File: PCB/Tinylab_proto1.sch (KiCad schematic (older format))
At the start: 73 parts, among them IC1 ATXMEGA16A4U-A, P1 SCOPE_OUT, P10 EXPANSION, P11 SWITCH, P2 USB_OTG, P3 DIG_OUT, P4 PDI/3V3, P5 SCOPE_OUT, P6 DAC_OUT, P7 PSU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

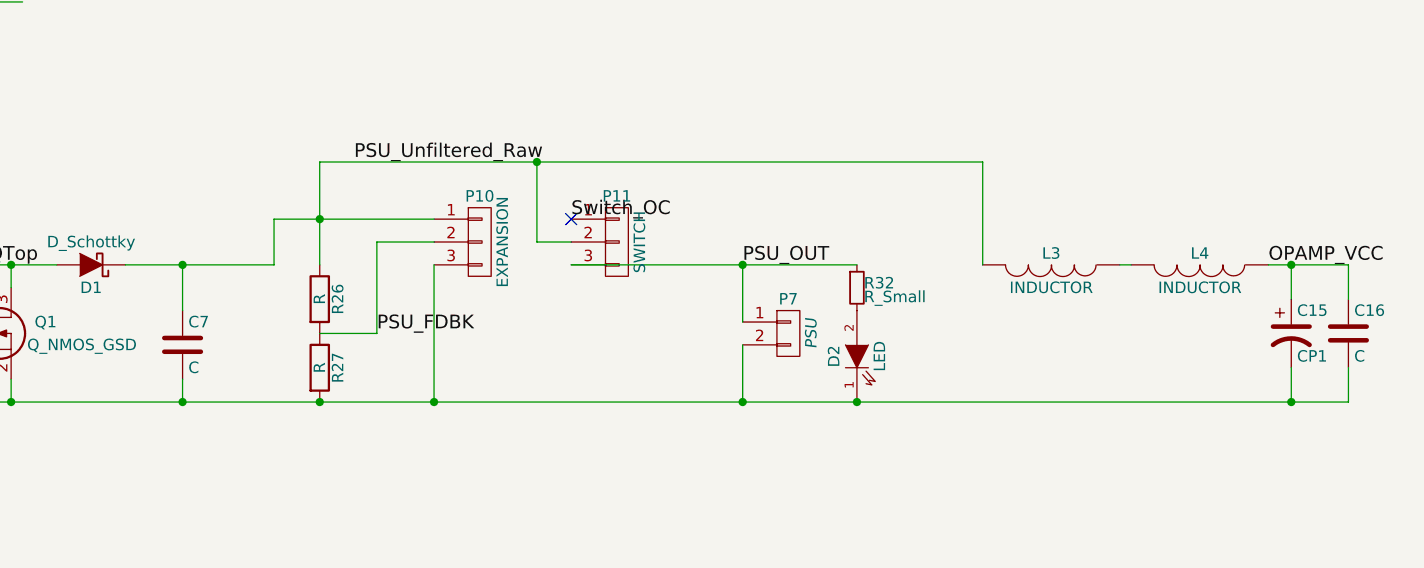
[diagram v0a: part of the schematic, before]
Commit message: Redoing the board
Signal gen and PSU wired in.  Very happy!
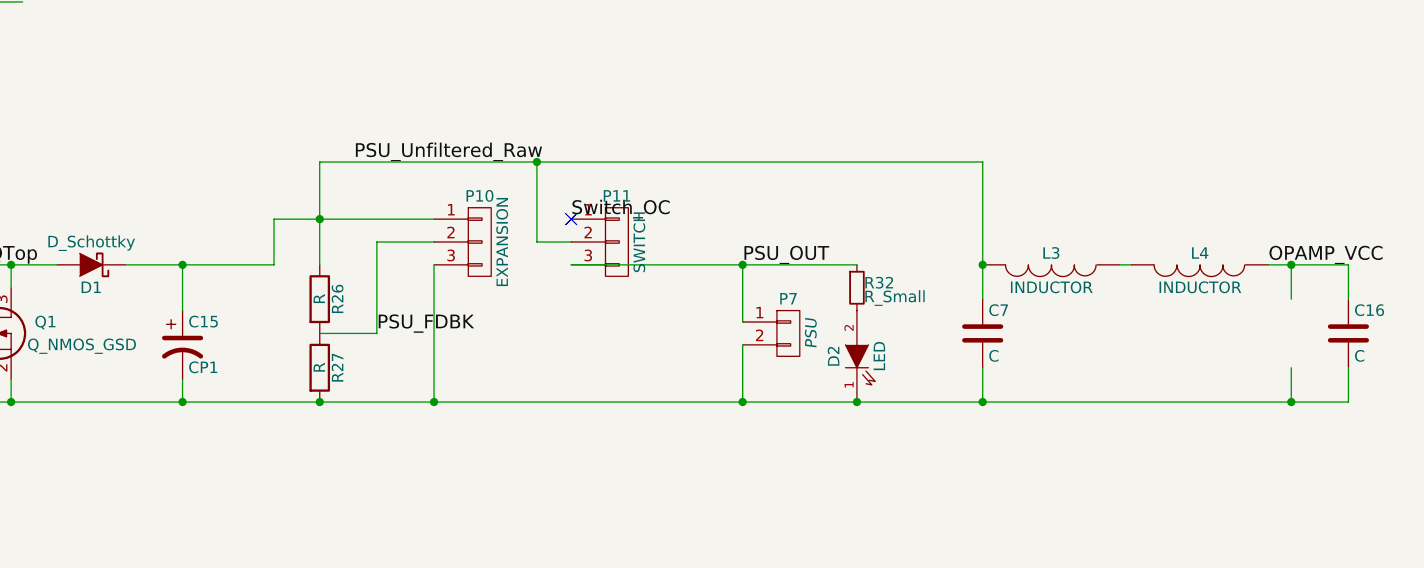
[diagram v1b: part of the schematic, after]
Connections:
- net OPAMP_VCC: no longer C15.1
- net PSU_Unfiltered_Raw: now also C15.1
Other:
- moved on the sheet: C15, C7
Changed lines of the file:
@@
 L CP1 C15
 U 1 1 560735FE
-P 16350 5350
-F 0 "C15" H 16375 5450 50  0000 L CNN
-F 1 "CP1" H 16375 5250 50  0000 L CNN
-F 2 "Capacitors_SMD:c_elec_4x5.3" H 16350 5350 60  0001 C CNN
-F 3 "" H 16350 5350 60  0000 C CNN
-	1    16350 5350
+P 11500 5400
+F 0 "C15" H 11525 5500 50  0000 L CNN
+F 1 "CP1" H 11525 5300 50  0000 L CNN
+F 2 "Capacitors_SMD:c_elec_4x5.3" H 11500 5400 60  0001 C CNN
+F 3 "" H 11500 5400 60  0000 C CNN
+	1    11500 5400
 	1    0    0    -1
 $EndComp
@@
 L C C7
 U 1 1 56E8E263
-P 11500 5400
-F 0 "C7" H 11525 5500 50  0000 L CNN
-F 1 "C" H 11525 5300 50  0000 L CNN
-F 2 "Capacitors_SMD:C_0603" H 11538 5250 30  0001 C CNN
-F 3 "" H 11500 5400 60  0000 C CNN
-	1    11500 5400
+P 15000 5350
+F 0 "C7" H 15025 5450 50  0000 L CNN
+F 1 "C" H 15025 5250 50  0000 L CNN
+F 2 "Capacitors_SMD:C_0603" H 15038 5200 30  0001 C CNN
+F 3 "" H 15000 5350 60  0000 C CNN
+	1    15000 5350
 	1    0    0    -1
 $EndComp
@@
 	16600 5050 16600 5200
 Wire Wire Line
-	16350 5200 16350 5050
-Wire Wire Line
-	16350 5650 16350 5500
-Wire Wire Line
 	12100 5350 12350 5350
 Connection ~ 10300 5350
@@
 	12100 4600 15000 4600
 Wire Wire Line
-	15000 4600 15000 5050
+	15000 4600 15000 5200
 Wire Wire Line
 	12100 4600 12100 5050
@@
 Text Label 11000 11550 0    60   ~ 0
 R23-R25
+Connection ~ 15000 5050
+Wire Wire Line
+	15000 5500 15000 5650
+Connection ~ 15000 5650
+Wire Wire Line
+	16350 5200 16350 5050
+Wire Wire Line
+	16350 5500 16350 5650
 $EndSCHEMATC

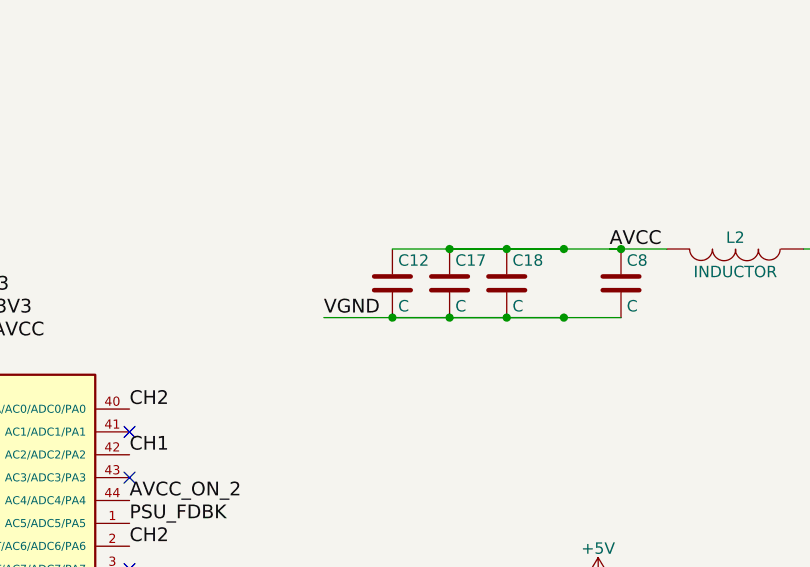
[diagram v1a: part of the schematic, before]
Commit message: FInished the board.
Just need to position balange pins.  Design seems tight, with really low
power supply distances.
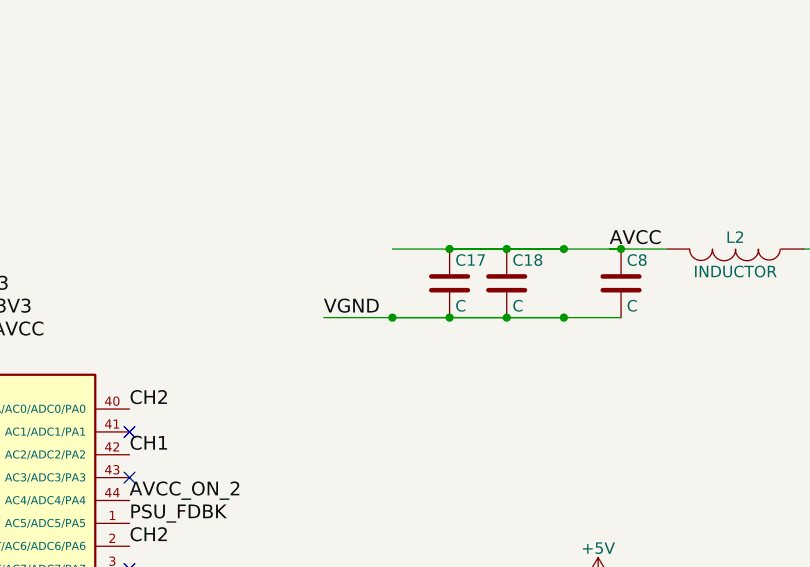
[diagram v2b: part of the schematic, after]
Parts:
- removed C12: C, Capacitors_SMD:C_0603, symbol C
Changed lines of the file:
@@
-$EndComp
-$Comp
-L C C12
-U 1 1 575646EC
-P 8200 3750
-F 0 "C12" H 8225 3850 50  0000 L CNN
-F 1 "C" H 8225 3650 50  0000 L CNN
-F 2 "Capacitors_SMD:C_0603" H 8238 3600 50  0001 C CNN
-F 3 "" H 8200 3750 50  0000 C CNN
-	1    8200 3750
-	1    0    0    -1
 $EndComp
 $Comp
@@
 Wire Wire Line
 	13950 5650 13950 5400
-Wire Wire Line
-	8200 3600 9200 3600
 Wire Wire Line
 	8450 3600 8950 3600
@@
 Wire Wire Line
 	16350 5500 16350 5650
+Wire Wire Line
+	8200 3600 9200 3600
 $EndSCHEMATC

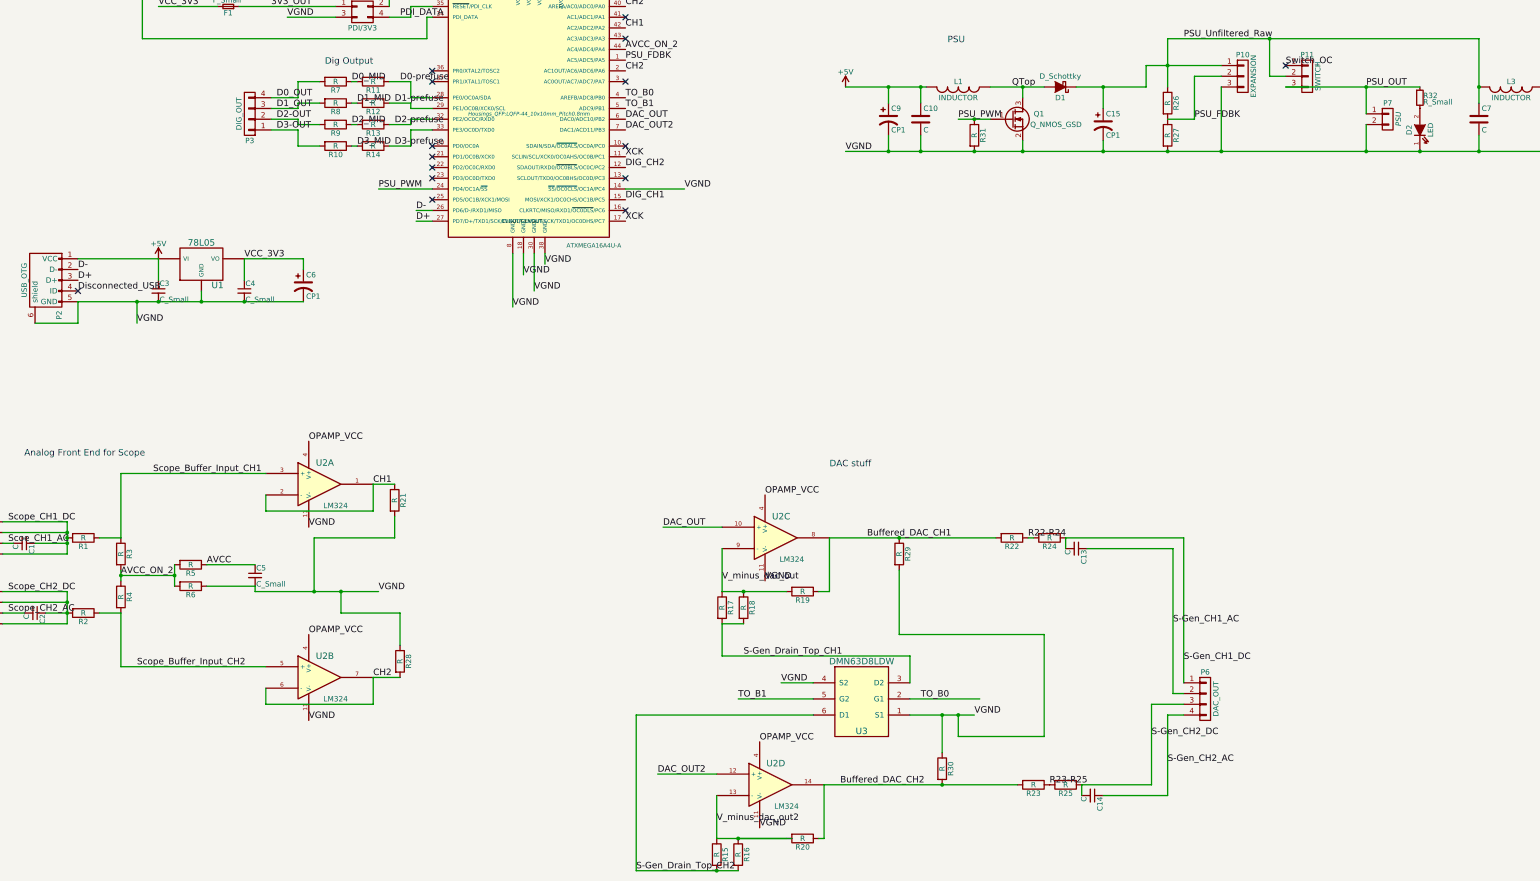
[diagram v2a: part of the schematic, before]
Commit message: Added more #defines to code
These #defines are located in desktop_settings.h and allow you to edit
how many samples are discarded per packet.  The idea was to use this to
test the MCU-side code and ensure that it doesn't corrupt a packet per
frame, but this seems to have magically disappeared (???).

I remember queueing USB transfers a long time ago, but can't remember
this having any success.  It's more likely to just be a random clock
skew issue that only appears on some boards - and it's only "fixed" on
the one particular test board I have in hand now.  I think.
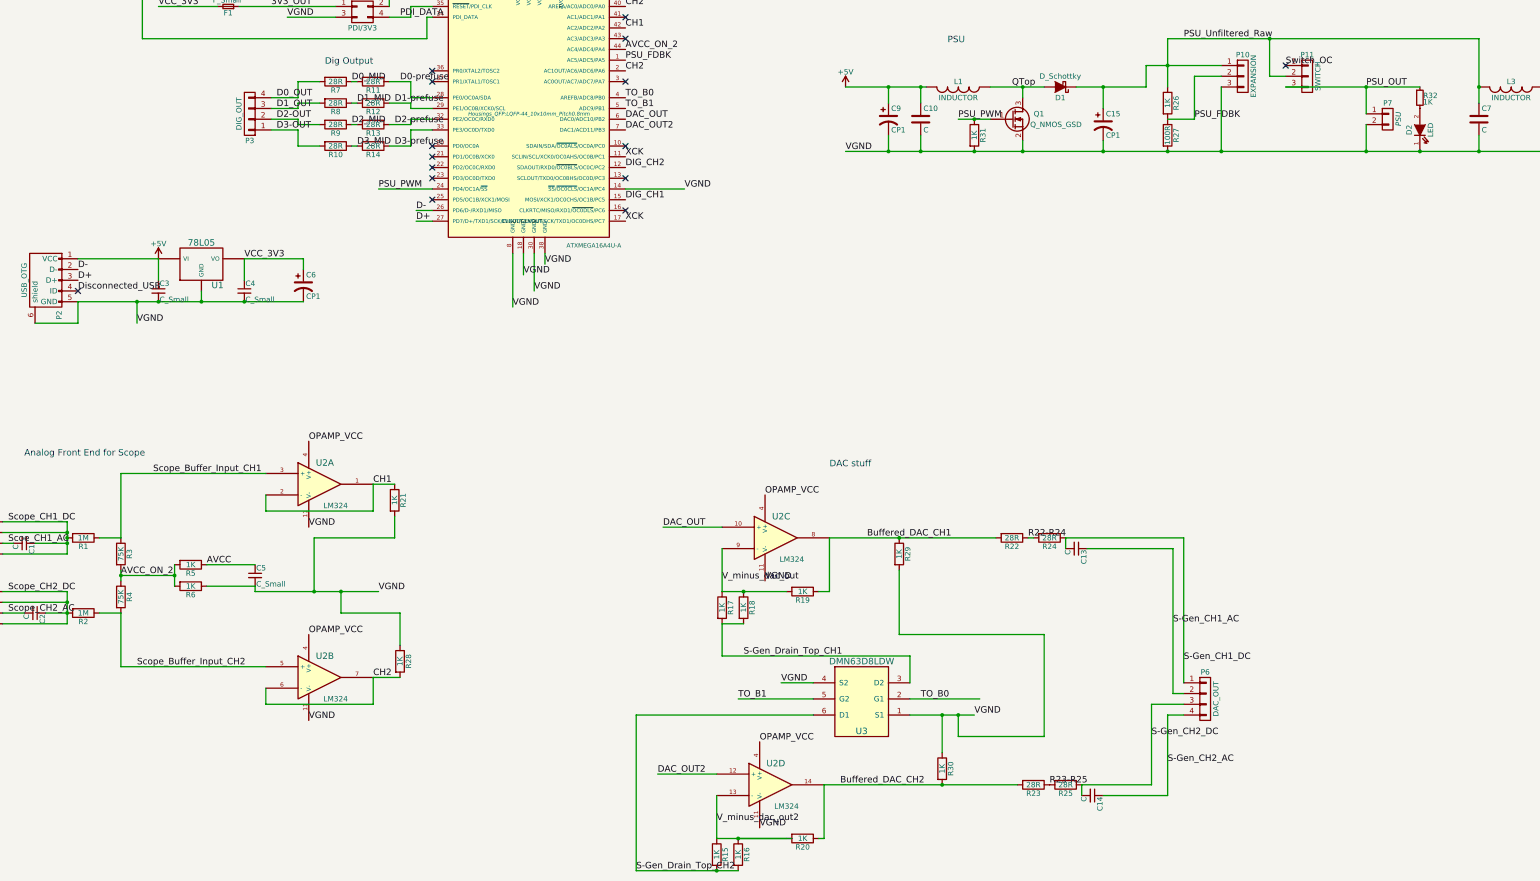
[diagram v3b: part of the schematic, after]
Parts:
- R1, R2: value R -> 1M
- R10, R11, R12, R13, R14, R22, R23, R24, R25, R7, R8, R9: value R -> 28R
- R15, R16, R17, R18, R19, R20, R21, R26, R28, R29, R30, R31, R5, R6: value R -> 1K
- R27: value R -> 100R
- R3, R4: value R -> 75K
- R32: value R_Small -> 1K
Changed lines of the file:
@@
 P 2000 9250
 F 0 "R1" V 2080 9250 50  0000 C CNN
-F 1 "R" V 2000 9250 50  0000 C CNN
+F 1 "1M" V 2000 9250 50  0000 C CNN
 F 2 "Resistors_SMD:R_0603" V 1930 9250 30  0001 C CNN
 F 3 "" H 2000 9250 30  0000 C CNN
@@
 P 2350 9400
 F 0 "R3" V 2430 9400 50  0000 C CNN
-F 1 "R" V 2350 9400 50  0000 C CNN
+F 1 "75K" V 2350 9400 50  0000 C CNN
 F 2 "Resistors_SMD:R_0603" V 2280 9400 30  0001 C CNN
 F 3 "" H 2350 9400 30  0000 C CNN
@@
 P 3000 9500
 F 0 "R5" V 3080 9500 50  0000 C CNN
-F 1 "R" V 3000 9500 50  0000 C CNN
+F 1 "1K" V 3000 9500 50  0000 C CNN
 F 2 "Resistors_SMD:R_0603" V 2930 9500 30  0001 C CNN
 F 3 "" H 3000 9500 30  0000 C CNN
@@
 P 3000 9700
 F 0 "R6" V 3080 9700 50  0000 C CNN
-F 1 "R" V 3000 9700 50  0000 C CNN
+F 1 "1K" V 3000 9700 50  0000 C CNN
 F 2 "Resistors_SMD:R_0603" V 2930 9700 30  0001 C CNN
 F 3 "" H 3000 9700 30  0000 C CNN
@@
 P 2350 9800
 F 0 "R4" V 2430 9800 50  0000 C CNN
-F 1 "R" V 2350 9800 50  0000 C CNN
+F 1 "75K" V 2350 9800 50  0000 C CNN
 F 2 "Resistors_SMD:R_0603" V 2280 9800 30  0001 C CNN
 F 3 "" H 2350 9800 30  0000 C CNN
@@
 P 2000 9950
 F 0 "R2" V 2080 9950 50  0000 C CNN
-F 1 "R" V 2000 9950 50  0000 C CNN
+F 1 "1M" V 2000 9950 50  0000 C CNN
 F 2 "Resistors_SMD:R_0603" V 1930 9950 30  0001 C CNN
 F 3 "" H 2000 9950 30  0000 C CNN
@@
 P 10650 9250
 F 0 "R22" V 10730 9250 50  0000 C CNN
-F 1 "R" V 10650 9250 50  0000 C CNN
+F 1 "28R" V 10650 9250 50  0000 C CNN
 F 2 "Resistors_SMD:R_0603" V 10580 9250 30  0001 C CNN
 F 3 "" H 10650 9250 30  0000 C CNN
@@
 P 11000 9250
 F 0 "R24" V 11080 9250 50  0000 C CNN
-F 1 "R" V 11000 9250 50  0000 C CNN
+F 1 "28R" V 11000 9250 50  0000 C CNN
 F 2 "Resistors_SMD:R_0603" V 10930 9250 30  0001 C CNN
 F 3 "" H 11000 9250 30  0000 C CNN
@@
 P 4700 5000
 F 0 "R11" V 4780 5000 50  0000 C CNN
-F 1 "R" V 4700 5000 50  0000 C CNN
+F 1 "28R" V 4700 5000 50  0000 C CNN
 F 2 "Resistors_SMD:R_0603" V 4630 5000 30  0001 C CNN
 F 3 "" H 4700 5000 30  0000 C CNN
@@
 P 4350 5000
 F 0 "R7" V 4430 5000 50  0000 C CNN
-F 1 "R" V 4350 5000 50  0000 C CNN
+F 1 "28R" V 4350 5000 50  0000 C CNN
 F 2 "Resistors_SMD:R_0603" V 4280 5000 30  0001 C CNN
 F 3 "" H 4350 5000 30  0000 C CNN
@@
 P 4700 5400
 F 0 "R13" V 4780 5400 50  0000 C CNN
-F 1 "R" V 4700 5400 50  0000 C CNN
+F 1 "28R" V 4700 5400 50  0000 C CNN
 F 2 "Resistors_SMD:R_0603" V 4630 5400 30  0001 C CNN
 F 3 "" H 4700 5400 30  0000 C CNN
@@
 P 4350 5400
 F 0 "R9" V 4430 5400 50  0000 C CNN
-F 1 "R" V 4350 5400 50  0000 C CNN
+F 1 "28R" V 4350 5400 50  0000 C CNN
 F 2 "Resistors_SMD:R_0603" V 4280 5400 30  0001 C CNN
 F 3 "" H 4350 5400 30  0000 C CNN
@@
 P 4700 5600
 F 0 "R14" V 4780 5600 50  0000 C CNN
-F 1 "R" V 4700 5600 50  0000 C CNN
+F 1 "28R" V 4700 5600 50  0000 C CNN
 F 2 "Resistors_SMD:R_0603" V 4630 5600 30  0001 C CNN
 F 3 "" H 4700 5600 30  0000 C CNN
@@
 P 4350 5600
 F 0 "R10" V 4430 5600 50  0000 C CNN
-F 1 "R" V 4350 5600 50  0000 C CNN
+F 1 "28R" V 4350 5600 50  0000 C CNN
 F 2 "Resistors_SMD:R_0603" V 4280 5600 30  0001 C CNN
 F 3 "" H 4350 5600 30  0000 C CNN
@@
 P 4700 5200
 F 0 "R12" V 4780 5200 50  0000 C CNN
-F 1 "R" V 4700 5200 50  0000 C CNN
+F 1 "28R" V 4700 5200 50  0000 C CNN
 F 2 "Resistors_SMD:R_0603" V 4630 5200 30  0001 C CNN
 F 3 "" H 4700 5200 30  0000 C CNN
@@
 P 4350 5200
 F 0 "R8" V 4430 5200 50  0000 C CNN
-F 1 "R" V 4350 5200 50  0000 C CNN
+F 1 "28R" V 4350 5200 50  0000 C CNN
 F 2 "Resistors_SMD:R_0603" V 4280 5200 30  0001 C CNN
 F 3 "" H 4350 5200 30  0000 C CNN
@@
 P 10850 11550
 F 0 "R23" V 10930 11550 50  0000 C CNN
-F 1 "R" V 10850 11550 50  0000 C CNN
+F 1 "28R" V 10850 11550 50  0000 C CNN
 F 2 "Resistors_SMD:R_0603" V 10780 11550 30  0001 C CNN
 F 3 "" H 10850 11550 30  0000 C CNN
@@
 P 11150 11550
 F 0 "R25" V 11230 11550 50  0000 C CNN
-F 1 "R" V 11150 11550 50  0000 C CNN
+F 1 "28R" V 11150 11550 50  0000 C CNN
 F 2 "Resistors_SMD:R_0603" V 11080 11550 30  0001 C CNN
 F 3 "" H 11150 11550 30  0000 C CNN
@@
 P 12100 5200
 F 0 "R26" V 12180 5200 50  0000 C CNN
-F 1 "R" V 12100 5200 50  0000 C CNN
+F 1 "1K" V 12100 5200 50  0000 C CNN
 F 2 "Resistors_SMD:R_0603" V 12030 5200 30  0001 C CNN
 F 3 "" H 12100 5200 30  0000 C CNN
@@
 P 12100 5500
 F 0 "R27" V 12180 5500 50  0000 C CNN
-F 1 "R" V 12100 5500 50  0000 C CNN
+F 1 "100R" V 12100 5500 50  0000 C CNN
 F 2 "Resistors_SMD:R_0603" V 12030 5500 30  0001 C CNN
 F 3 "" H 12100 5500 30  0000 C CNN
@@
 P 8700 9750
 F 0 "R19" V 8780 9750 50  0000 C CNN
-F 1 "R" V 8700 9750 50  0000 C CNN
+F 1 "1K" V 8700 9750 50  0000 C CNN
 F 2 "Resistors_SMD:R_0603" V 8630 9750 30  0001 C CNN
 F 3 "" H 8700 9750 30  0000 C CNN
@@
 P 7950 9900
 F 0 "R17" V 8030 9900 50  0000 C CNN
-F 1 "R" V 7950 9900 50  0000 C CNN
+F 1 "1K" V 7950 9900 50  0000 C CNN
 F 2 "Resistors_SMD:R_0603" V 7880 9900 30  0001 C CNN
 F 3 "" H 7950 9900 30  0000 C CNN
@@
 P 8150 9900
 F 0 "R18" V 8230 9900 50  0000 C CNN
-F 1 "R" V 8150 9900 50  0000 C CNN
+F 1 "1K" V 8150 9900 50  0000 C CNN
 F 2 "Resistors_SMD:R_0603" V 8080 9900 30  0001 C CNN
 F 3 "" H 8150 9900 30  0000 C CNN
@@
 P 8700 12050
 F 0 "R20" V 8780 12050 50  0000 C CNN
-F 1 "R" V 8700 12050 50  0000 C CNN
+F 1 "1K" V 8700 12050 50  0000 C CNN
 F 2 "Resistors_SMD:R_0603" V 8630 12050 30  0001 C CNN
 F 3 "" H 8700 12050 30  0000 C CNN
@@
 P 7900 12200
 F 0 "R15" V 7980 12200 50  0000 C CNN
-F 1 "R" V 7900 12200 50  0000 C CNN
+F 1 "1K" V 7900 12200 50  0000 C CNN
 F 2 "Resistors_SMD:R_0603" V 7830 12200 30  0001 C CNN
 F 3 "" H 7900 12200 30  0000 C CNN
@@
 P 8100 12200
 F 0 "R16" V 8180 12200 50  0000 C CNN
-F 1 "R" V 8100 12200 50  0000 C CNN
+F 1 "1K" V 8100 12200 50  0000 C CNN
 F 2 "Resistors_SMD:R_0603" V 8030 12200 30  0001 C CNN
 F 3 "" H 8100 12200 30  0000 C CNN
@@
 P 4900 8900
 F 0 "R21" V 4980 8900 50  0000 C CNN
-F 1 "R" V 4900 8900 50  0000 C CNN
+F 1 "1K" V 4900 8900 50  0000 C CNN
 F 2 "Resistors_SMD:R_0603" V 4830 8900 30  0001 C CNN
 F 3 "" H 4900 8900 30  0000 C CNN
@@
 P 4950 10400
 F 0 "R28" V 5030 10400 50  0000 C CNN
-F 1 "R" V 4950 10400 50  0000 C CNN
+F 1 "1K" V 4950 10400 50  0000 C CNN
 F 2 "Resistors_SMD:R_0603" V 4880 10400 30  0001 C CNN
 F 3 "" H 4950 10400 30  0000 C CNN
@@
 P 9600 9400
 F 0 "R29" V 9680 9400 50  0000 C CNN
-F 1 "R" V 9600 9400 50  0000 C CNN
+F 1 "1K" V 9600 9400 50  0000 C CNN
 F 2 "Resistors_SMD:R_0603" V 9530 9400 30  0001 C CNN
 F 3 "" H 9600 9400 30  0000 C CNN
@@
 P 10000 11400
 F 0 "R30" V 10080 11400 50  0000 C CNN
-F 1 "R" V 10000 11400 50  0000 C CNN
+F 1 "1K" V 10000 11400 50  0000 C CNN
 F 2 "Resistors_SMD:R_0603" V 9930 11400 30  0001 C CNN
 F 3 "" H 10000 11400 30  0000 C CNN
@@
 P 10300 5500
 F 0 "R31" V 10380 5500 50  0000 C CNN
-F 1 "R" V 10300 5500 50  0000 C CNN
+F 1 "1K" V 10300 5500 50  0000 C CNN
 F 2 "Resistors_SMD:R_0603" V 10230 5500 50  0001 C CNN
 F 3 "" H 10300 5500 50  0000 C CNN
@@
 P 14450 5150
 F 0 "R32" H 14480 5170 50  0000 L CNN
-F 1 "R_Small" H 14480 5110 50  0000 L CNN
+F 1 "1K" H 14480 5110 50  0000 L CNN
 F 2 "Resistors_SMD:R_0603" H 14450 5150 50  0001 C CNN
 F 3 "" H 14450 5150 50  0000 C CNN
